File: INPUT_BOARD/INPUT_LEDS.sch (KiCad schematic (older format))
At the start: 15 parts, among them Q1 MMBTA42, U3 TL074

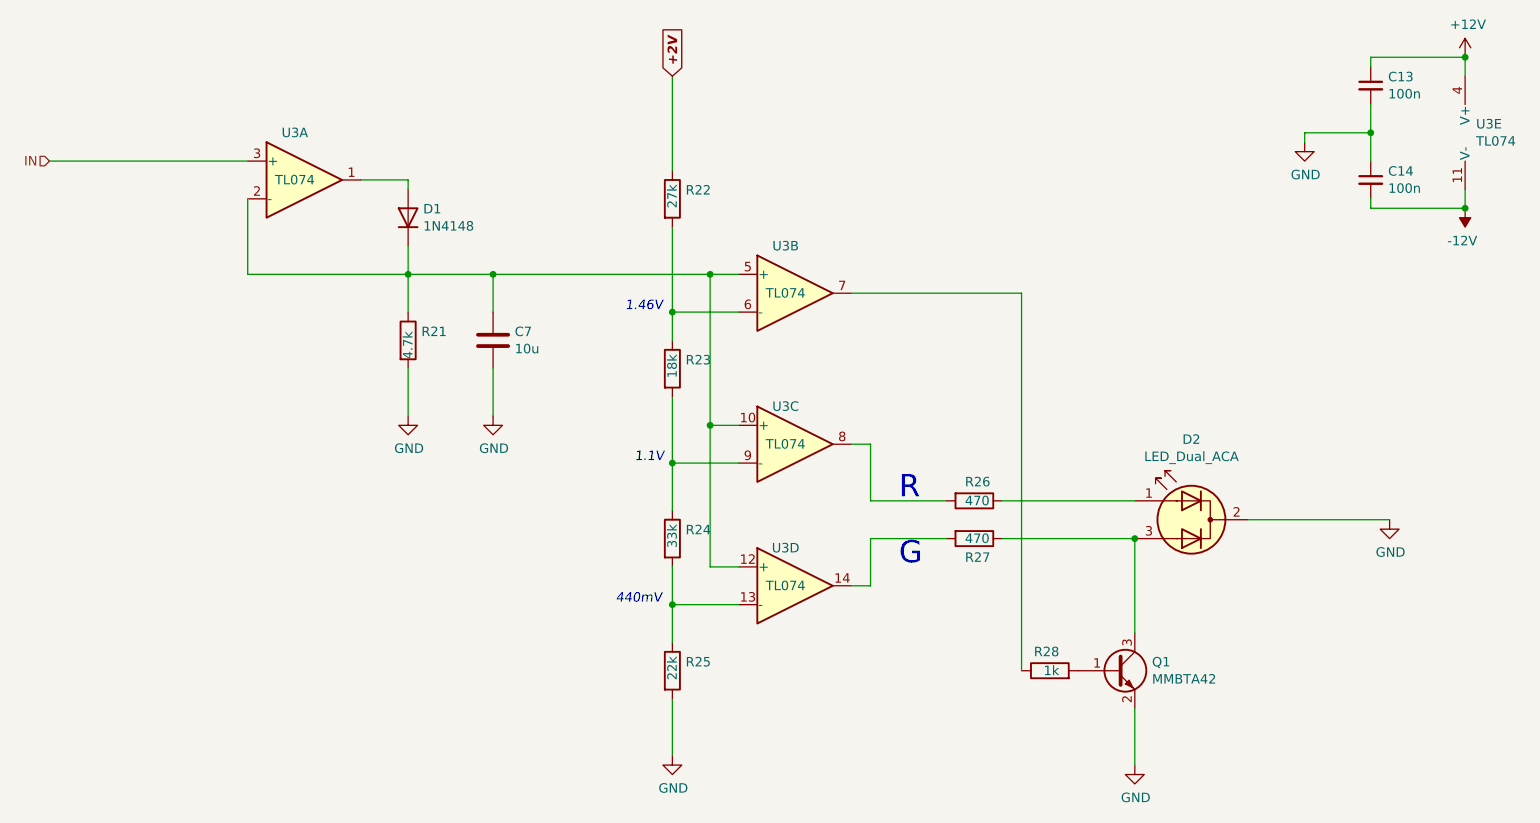
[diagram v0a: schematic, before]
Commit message: New series resistor values for LEDs
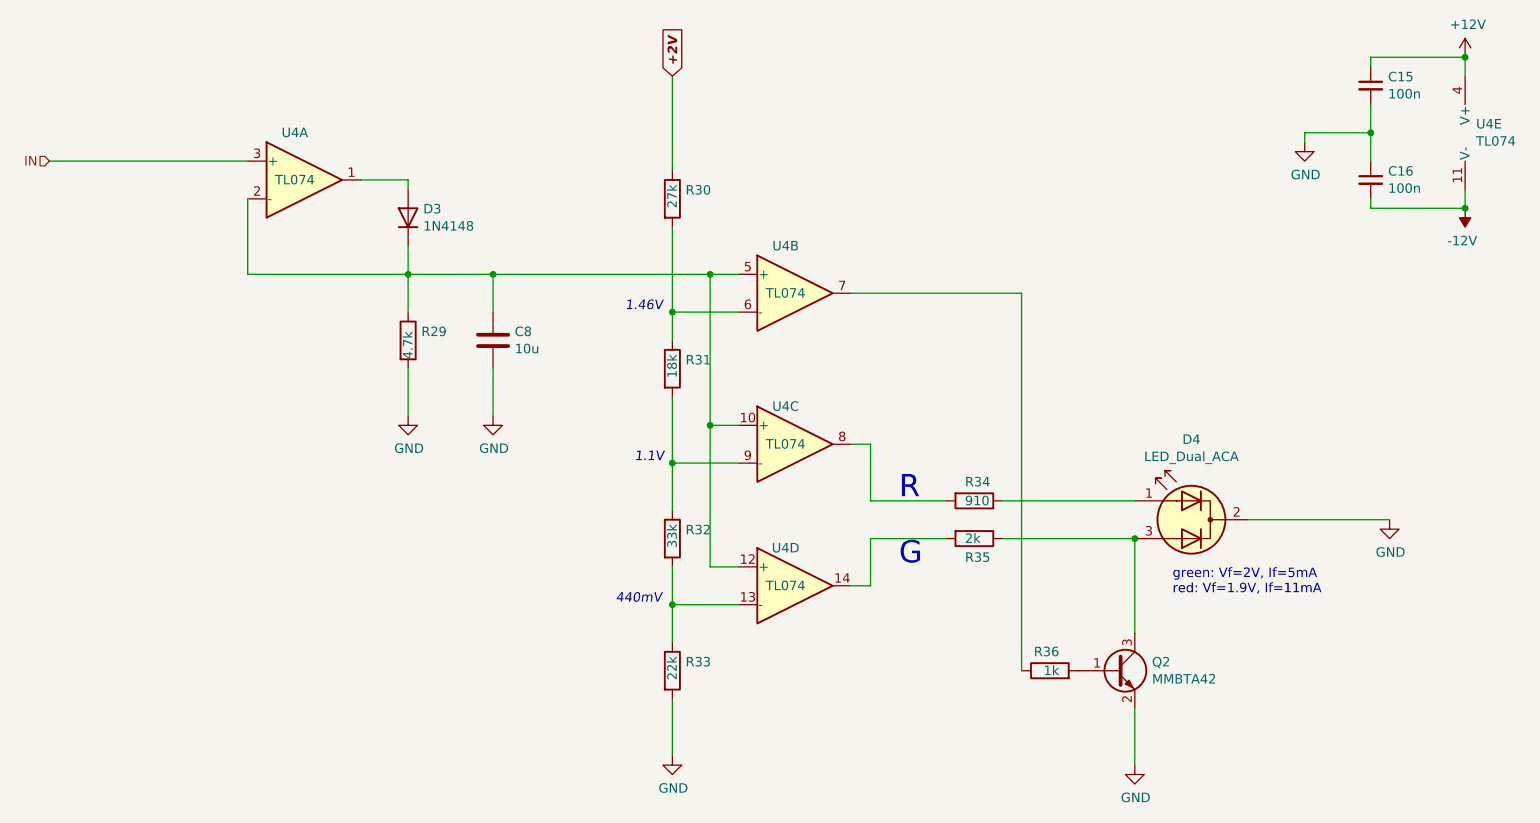
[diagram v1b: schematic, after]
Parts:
- R26: value 470 -> 910
- R27: value 470 -> 2k
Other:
- note added: "green: Vf=2V, If=5mA\nred: Vf=1.9V, If=11mA"
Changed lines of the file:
@@
 $Descr A4 11693 8268
 encoding utf-8
-Sheet 2 3
+Sheet 3 3
 Title ""
 Date "2021-05-26"
@@
 AR Path="/60C60815/60C26286" Ref="U3"  Part="1"
 AR Path="/60C211A9/60C26286" Ref="U4"  Part="1"
-F 0 "U3" H 2500 1850 50  0000 C CNN
+F 0 "U4" H 2500 1850 50  0000 C CNN
 F 1 "TL074" H 2500 1600 50  0000 C CNN
 F 2 "OHMCODER:TL074-SOIC-14" H 2500 1700 50  0001 C CNN
@@
 AR Path="/60C60815/60C28ED2" Ref="D1"  Part="1"
 AR Path="/60C211A9/60C28ED2" Ref="D3"  Part="1"
-F 0 "D1" V 3146 1720 50  0000 R CNN
+F 0 "D3" V 3146 1720 50  0000 R CNN
 F 1 "1N4148" V 3055 1720 50  0000 R CNN
 F 2 "Diode_SMD:D_SOD-123" H 3100 1625 50  0001 C CNN
@@
 AR Path="/60C60815/60C2C287" Ref="R21"  Part="1"
 AR Path="/60C211A9/60C2C287" Ref="R29"  Part="1"
-F 0 "R21" H 3170 2496 50  0000 L CNN
+F 0 "R29" H 3170 2496 50  0000 L CNN
 F 1 "4.7k" V 3100 2350 50  0000 L CNN
 F 2 "Resistor_SMD:R_0603_1608Metric_Pad0.98x0.95mm_HandSolder" V 3030 2450 50  0001 C CNN
@@
 AR Path="/60C60815/60C2F152" Ref="C7"  Part="1"
 AR Path="/60C211A9/60C2F152" Ref="C8"  Part="1"
-F 0 "C7" H 3665 2496 50  0000 L CNN
+F 0 "C8" H 3665 2496 50  0000 L CNN
 F 1 "10u" H 3665 2405 50  0000 L CNN
 F 2 "Capacitor_SMD:C_0603_1608Metric_Pad1.08x0.95mm_HandSolder" H 3588 2300 50  0001 C CNN
@@
 AR Path="/60C60815/60C305C0" Ref="U3"  Part="3"
 AR Path="/60C211A9/60C305C0" Ref="U4"  Part="3"
-F 0 "U3" H 5100 3200 50  0000 C CNN
+F 0 "U4" H 5100 3200 50  0000 C CNN
 F 1 "TL074" H 5100 3000 50  0000 C CNN
 F 2 "OHMCODER:TL074-SOIC-14" H 5100 3100 50  0001 C CNN
@@
 AR Path="/60C60815/60C34AED" Ref="U3"  Part="4"
 AR Path="/60C211A9/60C34AED" Ref="U4"  Part="4"
-F 0 "U3" H 5100 3950 50  0000 C CNN
+F 0 "U4" H 5100 3950 50  0000 C CNN
 F 1 "TL074" H 5100 3750 50  0000 C CNN
 F 2 "OHMCODER:TL074-SOIC-14" H 5100 3850 50  0001 C CNN
@@
 AR Path="/60C60815/60C384B8" Ref="R24"  Part="1"
 AR Path="/60C211A9/60C384B8" Ref="R32"  Part="1"
-F 0 "R24" H 4570 3546 50  0000 L CNN
+F 0 "R32" H 4570 3546 50  0000 L CNN
 F 1 "33k" V 4500 3450 50  0000 L CNN
 F 2 "Resistor_SMD:R_0603_1608Metric_Pad0.98x0.95mm_HandSolder" V 4430 3500 50  0001 C CNN
@@
 AR Path="/60C60815/60C3B4AB" Ref="R25"  Part="1"
 AR Path="/60C211A9/60C3B4AB" Ref="R33"  Part="1"
-F 0 "R25" H 4570 4246 50  0000 L CNN
+F 0 "R33" H 4570 4246 50  0000 L CNN
 F 1 "22k" V 4500 4150 50  0000 L CNN
 F 2 "Resistor_SMD:R_0603_1608Metric_Pad0.98x0.95mm_HandSolder" V 4430 4200 50  0001 C CNN
@@
 AR Path="/60C60815/60C3BA14" Ref="R22"  Part="1"
 AR Path="/60C211A9/60C3BA14" Ref="R30"  Part="1"
-F 0 "R22" H 4570 1746 50  0000 L CNN
+F 0 "R30" H 4570 1746 50  0000 L CNN
 F 1 "27k" V 4500 1650 50  0000 L CNN
 F 2 "Resistor_SMD:R_0603_1608Metric_Pad0.98x0.95mm_HandSolder" V 4430 1700 50  0001 C CNN
@@
 AR Path="/60C60815/60C3DFBD" Ref="#PWR019"  Part="1"
 AR Path="/60C211A9/60C3DFBD" Ref="#PWR026"  Part="1"
-F 0 "#PWR019" H 4500 4400 50  0001 C CNN
+F 0 "#PWR026" H 4500 4400 50  0001 C CNN
 F 1 "GND" H 4505 4477 50  0000 C CNN
 F 2 "" H 4500 4650 50  0001 C CNN
@@
 AR Path="/60C60815/60C3E8EA" Ref="#PWR018"  Part="1"
 AR Path="/60C211A9/60C3E8EA" Ref="#PWR025"  Part="1"
-F 0 "#PWR018" H 3550 2600 50  0001 C CNN
+F 0 "#PWR025" H 3550 2600 50  0001 C CNN
 F 1 "GND" H 3555 2677 50  0000 C CNN
 F 2 "" H 3550 2850 50  0001 C CNN
@@
 AR Path="/60C60815/60C3EB50" Ref="#PWR017"  Part="1"
 AR Path="/60C211A9/60C3EB50" Ref="#PWR024"  Part="1"
-F 0 "#PWR017" H 3100 2600 50  0001 C CNN
+F 0 "#PWR024" H 3100 2600 50  0001 C CNN
 F 1 "GND" H 3105 2677 50  0000 C CNN
 F 2 "" H 3100 2850 50  0001 C CNN
@@
 AR Path="/60C60815/60C3EF33" Ref="#PWR021"  Part="1"
 AR Path="/60C211A9/60C3EF33" Ref="#PWR028"  Part="1"
-F 0 "#PWR021" H 8300 3150 50  0001 C CNN
+F 0 "#PWR028" H 8300 3150 50  0001 C CNN
 F 1 "GND" H 8305 3227 50  0000 C CNN
 F 2 "" H 8300 3400 50  0001 C CNN
@@
 AR Path="/60C60815/60C42FD6" Ref="R26"  Part="1"
 AR Path="/60C211A9/60C42FD6" Ref="R34"  Part="1"
-F 0 "R26" V 6000 3250 50  0000 L CNN
-F 1 "470" V 6100 3250 50  0000 L CNN
+F 0 "R34" V 6000 3250 50  0000 L CNN
+F 1 "910" V 6100 3250 50  0000 L CNN
 F 2 "Resistor_SMD:R_0603_1608Metric_Pad0.98x0.95mm_HandSolder" V 6030 3300 50  0001 C CNN
 F 3 "~" H 6100 3300 50  0001 C CNN
@@
 AR Path="/60C60815/60C43AA8" Ref="R27"  Part="1"
 AR Path="/60C211A9/60C43AA8" Ref="R35"  Part="1"
-F 0 "R27" V 6200 3450 50  0000 L CNN
-F 1 "470" V 6100 3450 50  0000 L CNN
+F 0 "R35" V 6200 3450 50  0000 L CNN
+F 1 "2k" V 6100 3450 50  0000 L CNN
 F 2 "Resistor_SMD:R_0603_1608Metric_Pad0.98x0.95mm_HandSolder" V 6030 3500 50  0001 C CNN
 F 3 "~" H 6100 3500 50  0001 C CNN
@@
 AR Path="/60C60815/60C4B75A" Ref="U3"  Part="2"
 AR Path="/60C211A9/60C4B75A" Ref="U4"  Part="2"
-F 0 "U3" H 5100 2450 50  0000 C CNN
+F 0 "U4" H 5100 2450 50  0000 C CNN
 F 1 "TL074" H 5100 2200 50  0000 C CNN
 F 2 "OHMCODER:TL074-SOIC-14" H 5100 2300 50  0001 C CNN
@@
 AR Path="/60C60815/60C4F3DA" Ref="U3"  Part="5"
 AR Path="/60C211A9/60C4F3DA" Ref="U4"  Part="5"
-F 0 "U3" H 8758 1396 50  0000 L CNN
+F 0 "U4" H 8758 1396 50  0000 L CNN
 F 1 "TL074" H 8758 1305 50  0000 L CNN
 F 2 "OHMCODER:TL074-SOIC-14" H 8750 1450 50  0001 C CNN
@@
 AR Path="/60C60815/60C51DC8" Ref="#PWR023"  Part="1"
 AR Path="/60C211A9/60C51DC8" Ref="#PWR030"  Part="1"
-F 0 "#PWR023" H 8700 1850 50  0001 C CNN
+F 0 "#PWR030" H 8700 1850 50  0001 C CNN
 F 1 "-12V" H 8715 1923 50  0000 C CNN
 F 2 "" H 8700 1750 50  0001 C CNN
@@
 AR Path="/60C60815/60C52C1A" Ref="#PWR022"  Part="1"
 AR Path="/60C211A9/60C52C1A" Ref="#PWR029"  Part="1"
-F 0 "#PWR022" H 8700 800 50  0001 C CNN
+F 0 "#PWR029" H 8700 800 50  0001 C CNN
 F 1 "+12V" H 8715 1123 50  0000 C CNN
 F 2 "" H 8700 950 50  0001 C CNN
@@
 AR Path="/60C60815/612ADEDE" Ref="R23"  Part="1"
 AR Path="/60C211A9/612ADEDE" Ref="R31"  Part="1"
-F 0 "R23" H 4570 2646 50  0000 L CNN
+F 0 "R31" H 4570 2646 50  0000 L CNN
 F 1 "18k" V 4500 2550 50  0000 L CNN
 F 2 "Resistor_SMD:R_0603_1608Metric_Pad0.98x0.95mm_HandSolder" V 4430 2600 50  0001 C CNN
@@
 AR Path="/60C60815/60C8A712" Ref="D2"  Part="1"
 AR Path="/60C211A9/60C8A712" Ref="D4"  Part="1"
-F 0 "D2" H 7250 3825 50  0000 C CNN
+F 0 "D4" H 7250 3825 50  0000 C CNN
 F 1 "LED_Dual_ACA" H 7250 3734 50  0000 C CNN
 F 2 "LED_THT:LED_D3.0mm-3" H 7250 3400 50  0001 C CNN
@@
 AR Path="/60C60815/60C98503" Ref="R28"  Part="1"
 AR Path="/60C211A9/60C98503" Ref="R36"  Part="1"
-F 0 "R28" V 6600 4150 50  0000 L CNN
+F 0 "R36" V 6600 4150 50  0000 L CNN
 F 1 "1k" V 6500 4150 50  0000 L CNN
 F 2 "Resistor_SMD:R_0603_1608Metric_Pad0.98x0.95mm_HandSolder" V 6430 4200 50  0001 C CNN
@@
 AR Path="/60C60815/60CA25AD" Ref="#PWR020"  Part="1"
 AR Path="/60C211A9/60CA25AD" Ref="#PWR027"  Part="1"
-F 0 "#PWR020" H 6950 4450 50  0001 C CNN
+F 0 "#PWR027" H 6950 4450 50  0001 C CNN
 F 1 "GND" H 6955 4527 50  0000 C CNN
 F 2 "" H 6950 4700 50  0001 C CNN
@@
 AR Path="/60C60815/60CD1243" Ref="Q1"  Part="1"
 AR Path="/60C211A9/60CD1243" Ref="Q2"  Part="1"
-F 0 "Q1" H 7041 4246 50  0000 L CNN
+F 0 "Q2" H 7041 4246 50  0000 L CNN
 F 1 "MMBTA42" H 7041 4155 50  0000 L CNN
 F 2 "Package_TO_SOT_SMD:SOT-23" H 7050 4125 50  0001 L CIN
@@
 AR Path="/60C60815/60FE6B82" Ref="C13"  Part="1"
 AR Path="/60C211A9/60FE6B82" Ref="C15"  Part="1"
-F 0 "C13" H 8292 1146 50  0000 L CNN
+F 0 "C15" H 8292 1146 50  0000 L CNN
 F 1 "100n" H 8292 1055 50  0000 L CNN
 F 2 "Capacitor_SMD:C_0603_1608Metric_Pad1.08x0.95mm_HandSolder" H 8200 1100 50  0001 C CNN
@@
 AR Path="/60C60815/60FE79BA" Ref="C14"  Part="1"
 AR Path="/60C211A9/60FE79BA" Ref="C16"  Part="1"
-F 0 "C14" H 8292 1646 50  0000 L CNN
+F 0 "C16" H 8292 1646 50  0000 L CNN
 F 1 "100n" H 8292 1555 50  0000 L CNN
 F 2 "Capacitor_SMD:C_0603_1608Metric_Pad1.08x0.95mm_HandSolder" H 8200 1600 50  0001 C CNN
@@
 AR Path="/60C60815/60FEC619" Ref="#PWR0106"  Part="1"
 AR Path="/60C211A9/60FEC619" Ref="#PWR0107"  Part="1"
-F 0 "#PWR0106" H 7850 1150 50  0001 C CNN
+F 0 "#PWR0107" H 7850 1150 50  0001 C CNN
 F 1 "GND" H 7855 1227 50  0000 C CNN
 F 2 "" H 7850 1400 50  0001 C CNN
@@
 	1    0    0    -1
 $EndComp
+Text Notes 7150 3800 0    50   ~ 0
+green: Vf=2V, If=5mA\nred: Vf=1.9V, If=11mA
 $EndSCHEMATC
